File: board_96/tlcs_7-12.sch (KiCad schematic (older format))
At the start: 66 parts, among them U4 TLC5941, U5 TLC5941, U6 TLC5941, U7 TLC5941, U8 TLC5941, U9 TLC5941

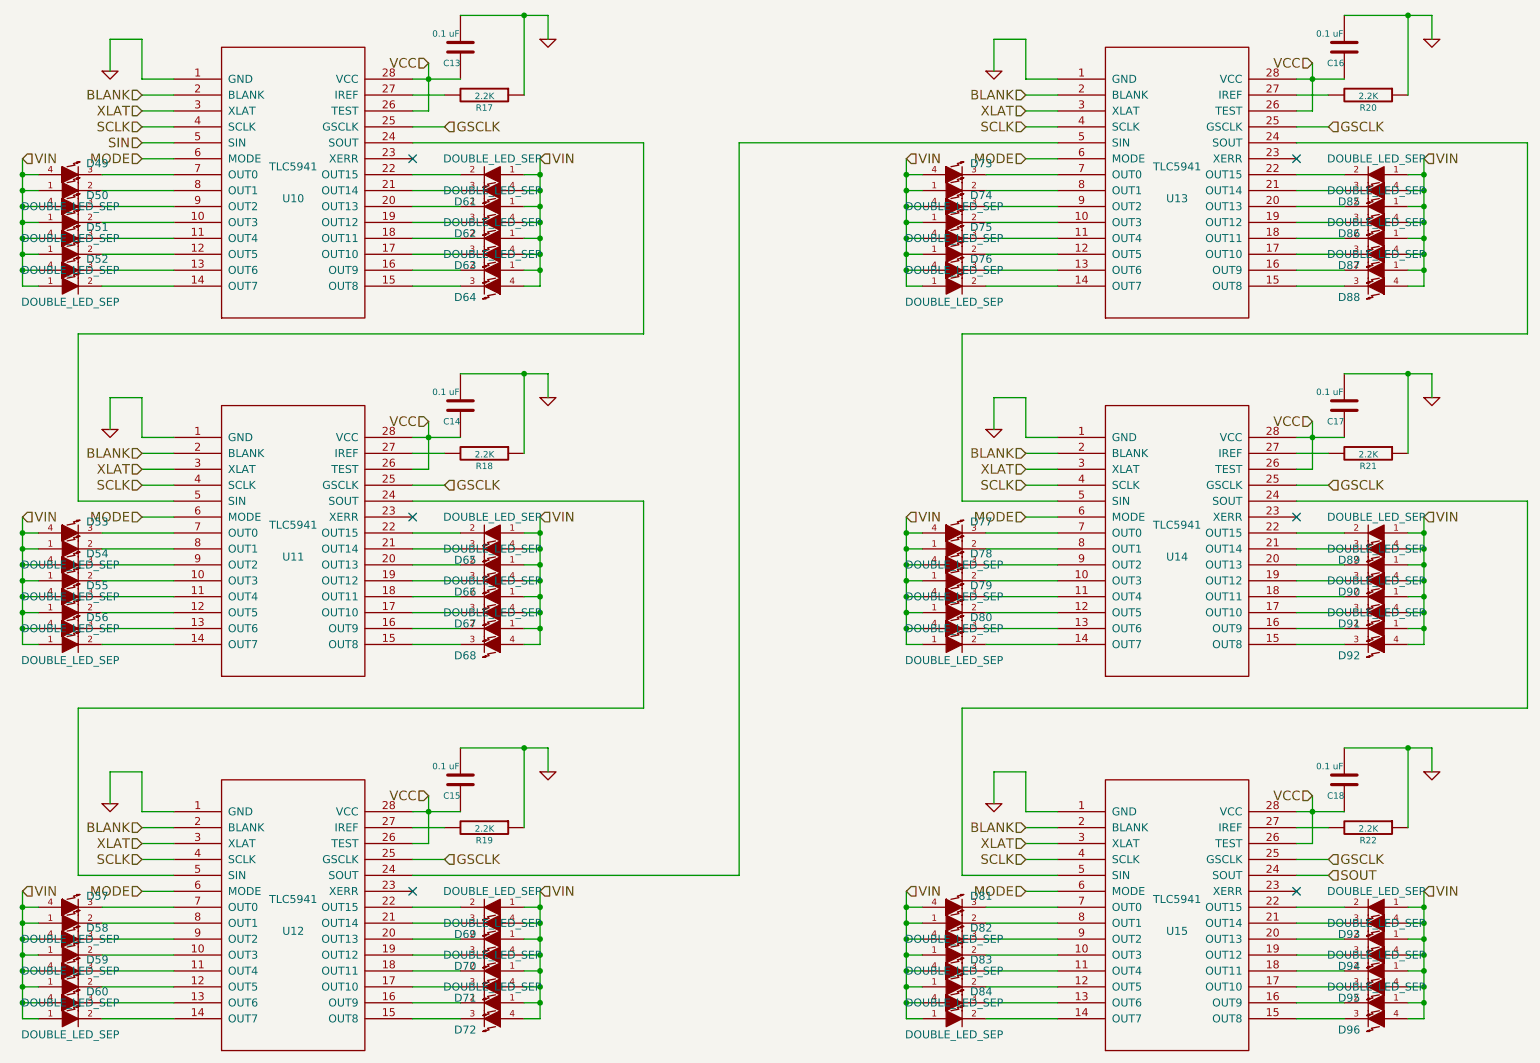
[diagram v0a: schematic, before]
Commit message: Made board_24_v2 which uses PCB-mounted LED sockets and updated various issues on board_96 as well. These PCBs were ordered around 7/1/14.
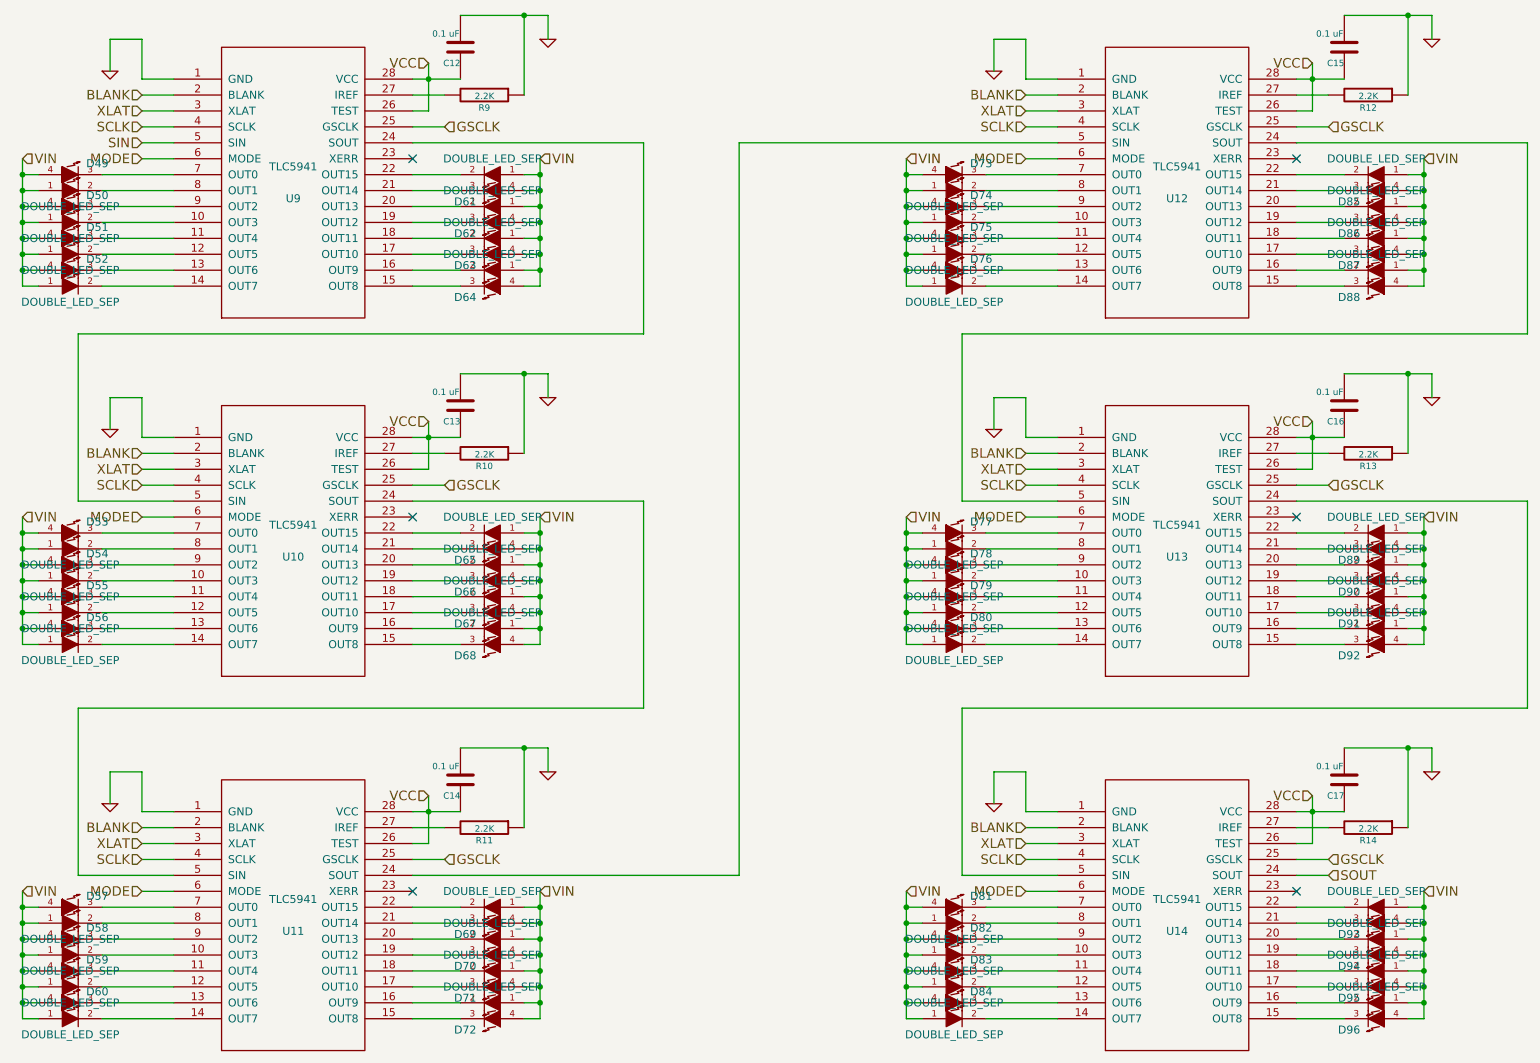
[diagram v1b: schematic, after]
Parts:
- removed C10, C11, C7, C9: 0.1 uF, ~, symbol C
- removed D1, D10, D11, D13, D14, D15, D18, D20, D21, D22, D24, D25, D26, D27, D28, D29, D30, D35, D36, D37, D38, D4, D44, D45, D46, D47, D48, D5, D6, D7, D8, D9: DOUBLE_LED_SEP, ~, symbol DOUBLE_LED_SEP
- removed R12, R15, R16: 2.2K, ~, symbol R
- removed U4, U5, U7, U8: TLC5941, MODULE, symbol TLC5941
- added C14, C15, C16, C17: 0.1 uF, SM0805, symbol C
- added D49, D52, D53, D54, D55, D56, D57, D58, D59, D61, D62, D63, D66, D68, D69, D70, D72, D73, D74, D75, D76, D77, D78, D83, D84, D85, D86, D92, D93, D94, D95, D96: DOUBLE_LED_SEP, SMD_0805_4PIN, symbol DOUBLE_LED_SEP
- added R10, R14, R9: 2.2K, SM0805, symbol R
- added U10, U12, U13, U14: TLC5941, TLC5940_FIXED, symbol TLC5941
- C12, R11, R13: footprint ~ -> SM0805
- C13: renamed from C8; footprint ~ -> SM0805
- D50: renamed from D2; footprint ~ -> SMD_0805_4PIN
- D51: renamed from D3; footprint ~ -> SMD_0805_4PIN
- D60: renamed from D12; footprint ~ -> SMD_0805_4PIN
- D64: renamed from D16; footprint ~ -> SMD_0805_4PIN
- D65: renamed from D17; footprint ~ -> SMD_0805_4PIN
- D67: renamed from D19; footprint ~ -> SMD_0805_4PIN
- D71: renamed from D23; footprint ~ -> SMD_0805_4PIN
- D79: renamed from D31; footprint ~ -> SMD_0805_4PIN
- D80: renamed from D32; footprint ~ -> SMD_0805_4PIN
- D81: renamed from D33; footprint ~ -> SMD_0805_4PIN
- D82: renamed from D34; footprint ~ -> SMD_0805_4PIN
- D87: renamed from D39; footprint ~ -> SMD_0805_4PIN
- D88: renamed from D40; footprint ~ -> SMD_0805_4PIN
- D89: renamed from D41; footprint ~ -> SMD_0805_4PIN
- D90: renamed from D42; footprint ~ -> SMD_0805_4PIN
- D91: renamed from D43; footprint ~ -> SMD_0805_4PIN
- R12: renamed from R14; footprint ~ -> SM0805
- U11: renamed from U6; footprint MODULE -> TLC5940_FIXED
- U9: footprint MODULE -> TLC5940_FIXED
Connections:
- net BLANK: now also U10.2 (BLANK), U12.2 (BLANK), U13.2 (BLANK), U14.2 (BLANK)
- net GND: now also C14.2, C15.2, C16.2, C17.2, R10.1, R14.1, R9.1, U10.1 (GND), U12.1 (GND), U13.1 (GND), U14.1 (GND)
- net GSCLK: now also U10.25 (GSCLK), U12.25 (GSCLK), U13.25 (GSCLK), U14.25 (GSCLK)
- net MODE: now also U10.6 (MODE), U12.6 (MODE), U13.6 (MODE), U14.6 (MODE)
- net SCLK: now also U10.4 (SCLK), U12.4 (SCLK), U13.4 (SCLK), U14.4 (SCLK)
- net SIN: now also U9.5 (SIN)
- net SOUT: now also U14.24 (SOUT); no longer U9.24 (SOUT)
- net VCC: now also C14.1, C15.1, C16.1, C17.1, U10.26 (TEST), U10.28 (VCC), U12.26 (TEST), U12.28 (VCC), U13.26 (TEST), U13.28 (VCC), U14.26 (TEST), U14.28 (VCC)
- net VIN: now also D49.1, D49.4, D52.1, D52.4, D53.1, D53.4, D54.1, D54.4, D55.1, D55.4, D56.1, D56.4, D57.1, D57.4, D58.1, D58.4, D59.1, D59.4, D61.1, D61.4, D62.1, D62.4, D63.1, D63.4, D66.1, D66.4, D68.1, D68.4, D69.1, D69.4, D70.1, D70.4, D72.1, D72.4, D73.1, D73.4, D74.1, D74.4, D75.1, D75.4, D76.1, D76.4, D77.1, D77.4, D78.1, D78.4, D83.1, D83.4, D84.1, D84.4, D85.1, D85.4, D86.1, D86.4, D92.1, D92.4, D93.1, D93.4, D94.1, D94.4, D95.1, D95.4, D96.1, D96.4
- net XLAT: now also U10.3 (XLAT), U12.3 (XLAT), U13.3 (XLAT), U14.3 (XLAT)
- net at U11.10 (OUT3): now also D58.2
- net at U11.11 (OUT4): now also D59.3
- net at U11.12 (OUT5): now also D59.2
- net at U11.15 (OUT8): now also D72.3
- net at U11.16 (OUT9): now also D72.2
- net at U11.19 (OUT12): now also D70.3
- net at U11.20 (OUT13): now also D70.2
- net at U11.21 (OUT14): now also D69.3
- net at U11.22 (OUT15): now also D69.2
- net at U11.24 (SOUT): now also U12.5 (SIN)
- net at U11.27 (IREF): now also R11.2; no longer R13.2
- net at U11.5 (SIN): now also U10.24 (SOUT)
- net at U11.7 (OUT0): now also D57.3
- net at U11.8 (OUT1): now also D57.2
- net at U11.9 (OUT2): now also D58.3
- net at D67.3: now also U10.17 (OUT10)
- net at D67.2: now also U10.18 (OUT11)
- net at D65.3: now also U10.21 (OUT14)
- net at D65.2: now also U10.22 (OUT15)
- net at D50.2: now also U9.10 (OUT3)
- net at D51.3: now also U9.11 (OUT4)
- net at D51.2: now also U9.12 (OUT5)
- net at D64.3: now also U9.15 (OUT8)
- net at D64.2: now also U9.16 (OUT9)
- net at D50.3: now also U9.9 (OUT2)
- net at D82.2: now also U14.10 (OUT3); no longer U9.10 (OUT3)
- net at U9.13 (OUT6): now also D52.3
- net at U9.14 (OUT7): now also D52.2
- net at U9.17 (OUT10): now also D63.3
- net at U9.18 (OUT11): now also D63.2
- net at U9.19 (OUT12): now also D62.3
- net at U9.20 (OUT13): now also D62.2
- net at U9.21 (OUT14): now also D61.3
- net at U9.22 (OUT15): now also D61.2
- net at U9.27 (IREF): now also R9.2
- net at D81.3: now also U14.7 (OUT0); no longer U9.7 (OUT0)
- net at D81.2: now also U14.8 (OUT1); no longer U9.8 (OUT1)
- net at D82.3: now also U14.9 (OUT2); no longer U9.9 (OUT2)
- net at D79.3: now also U13.11 (OUT4)
- net at D79.2: now also U13.12 (OUT5)
- net at D80.3: now also U13.13 (OUT6)
- net at D80.2: now also U13.14 (OUT7)
- net at D91.3: now also U13.17 (OUT10)
- net at D91.2: now also U13.18 (OUT11)
- net at D90.3: now also U13.19 (OUT12)
- net at D90.2: now also U13.20 (OUT13)
- net at D89.3: now also U13.21 (OUT14)
- net at D89.2: now also U13.22 (OUT15)
- net at R12.2: now also U12.27 (IREF)
- net at D88.3: now also U12.15 (OUT8)
- net at D88.2: now also U12.16 (OUT9)
- net at D87.3: now also U12.17 (OUT10)
- net at D87.2: now also U12.18 (OUT11)
- new net: D54.2, U10.10 (OUT3)
- new net: D55.3, U10.11 (OUT4)
- new net: D55.2, U10.12 (OUT5)
- new net: D56.3, U10.13 (OUT6)
- new net: D56.2, U10.14 (OUT7)
- new net: D68.3, U10.15 (OUT8)
- new net: D68.2, U10.16 (OUT9)
- new net: D66.3, U10.19 (OUT12)
- new net: D66.2, U10.20 (OUT13)
- new net: R10.2, U10.27 (IREF)
- new net: U10.5 (SIN), U9.24 (SOUT)
- new net: D53.3, U10.7 (OUT0)
- new net: D53.2, U10.8 (OUT1)
- new net: D54.3, U10.9 (OUT2)
- new net: D49.3, U9.7 (OUT0)
- new net: D49.2, U9.8 (OUT1)
- new net: D83.3, U14.11 (OUT4)
- new net: D83.2, U14.12 (OUT5)
- new net: D84.3, U14.13 (OUT6)
- new net: D84.2, U14.14 (OUT7)
- new net: D96.3, U14.15 (OUT8)
- new net: D96.2, U14.16 (OUT9)
- new net: D95.3, U14.17 (OUT10)
- new net: D95.2, U14.18 (OUT11)
- new net: D94.3, U14.19 (OUT12)
- new net: D94.2, U14.20 (OUT13)
- new net: D93.3, U14.21 (OUT14)
- new net: D93.2, U14.22 (OUT15)
- new net: R14.2, U14.27 (IREF)
- new net: U13.24 (SOUT), U14.5 (SIN)
- new net: D78.2, U13.10 (OUT3)
- new net: D92.3, U13.15 (OUT8)
- new net: D92.2, U13.16 (OUT9)
- new net: R13.2, U13.27 (IREF)
- new net: U12.24 (SOUT), U13.5 (SIN)
- new net: D77.3, U13.7 (OUT0)
- new net: D77.2, U13.8 (OUT1)
- new net: D78.3, U13.9 (OUT2)
- new net: D74.2, U12.10 (OUT3)
- new net: D75.3, U12.11 (OUT4)
- new net: D75.2, U12.12 (OUT5)
- new net: D76.3, U12.13 (OUT6)
- new net: D76.2, U12.14 (OUT7)
- new net: D86.3, U12.19 (OUT12)
- new net: D86.2, U12.20 (OUT13)
- new net: D85.3, U12.21 (OUT14)
- new net: D85.2, U12.22 (OUT15)
- new net: D73.3, U12.7 (OUT0)
- new net: D73.2, U12.8 (OUT1)
- new net: D74.3, U12.9 (OUT2)
